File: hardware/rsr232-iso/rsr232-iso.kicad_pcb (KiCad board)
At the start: 2 copper layers, 51 x 23 mm, 17 parts, among them J1 Serial, J2 PWR, J3 data, U1 MAX3232, U2 TLP2358, U3 TLP2358

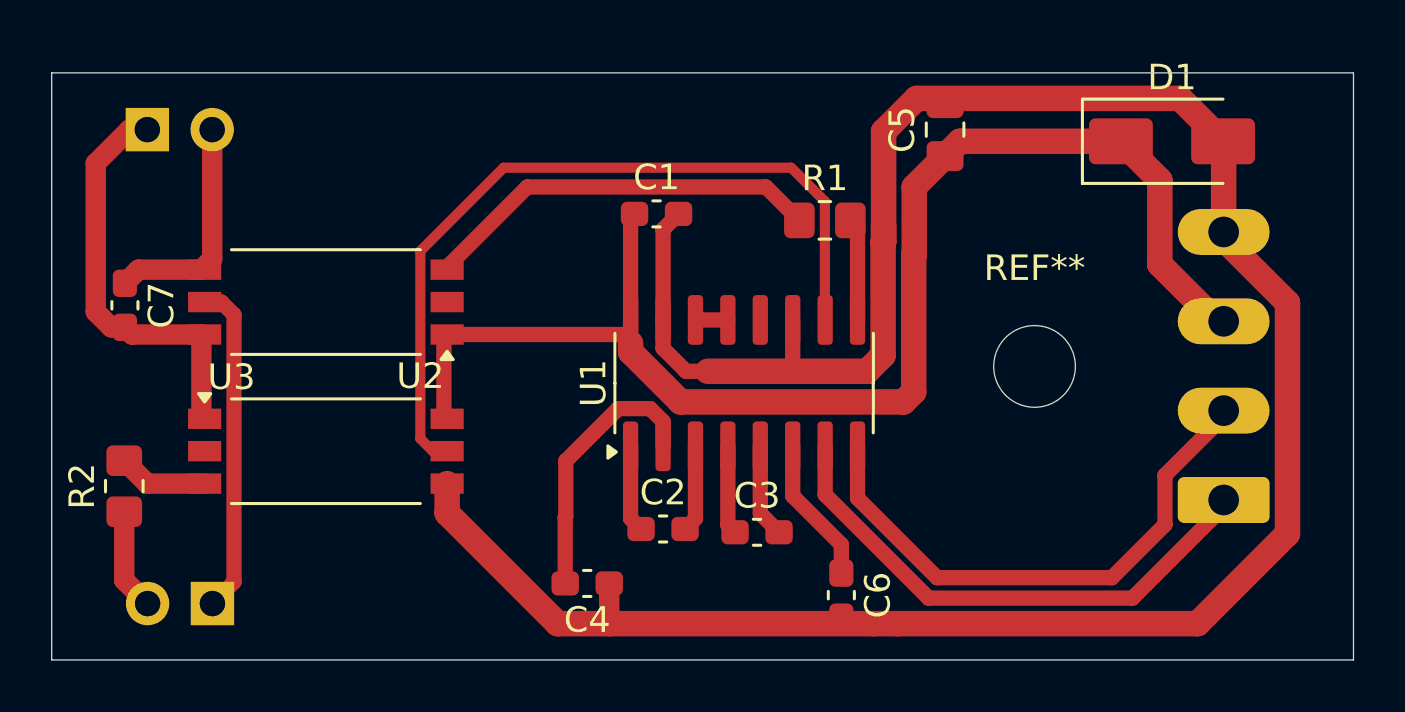
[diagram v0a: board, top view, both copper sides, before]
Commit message: Better clearance for mounting hole precise position for connectors
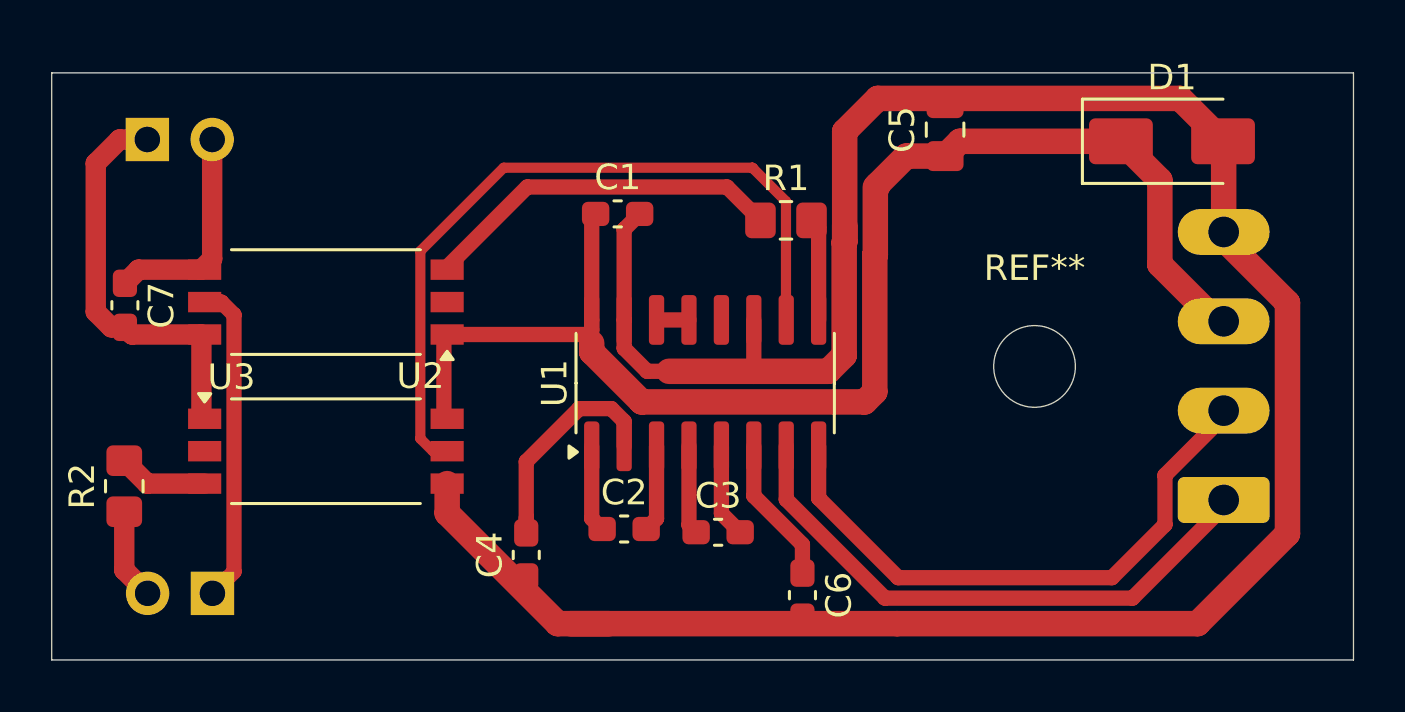
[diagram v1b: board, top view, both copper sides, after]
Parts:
- moved C4 2.64 mm to (143.1, 125.7), turned to 90 degrees
- moved C1 1.52 mm to (146.7, 112.4)
- moved C2 1.52 mm to (146.9, 124.7)
- moved C6 1.52 mm to (153.9, 127.3)
- moved R1 1.52 mm to (153.3, 112.6)
- moved U1 1.52 mm to (150.1, 119.0)
- moved C3 1.52 mm to (150.6, 124.8)
- moved J3 0.40 mm to (130.8, 127.2)
- moved J2 0.39 mm to (128.3, 109.5)
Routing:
- net /RS232tx: track 20.7 -> 22.3 mm
- net Net-(U2-K): track 15.8 -> 14.3 mm
- net /RS232rx: track 21.8 -> 23.3 mm
- net GND: track 96.1 -> 97.6 mm
- net Net-(U1-T2IN): track 31.0 -> 29.6 mm
- net Net-(U1-VS+): track 10.7 -> 9.28 mm

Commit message: Use a 2DIB1411F isolator instead of 2 optocouplers
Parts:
- removed R1: 330, Resistor_SMD:R_0805_2012Metric_Pad1.20x1.40mm_HandSolder
- removed R2: 220, Resistor_SMD:R_0805_2012Metric_Pad1.20x1.40mm_HandSolder
- removed REF**: MountingHole_3.2mm_M3_ISO7380, MountingHole:MountingHole_3.2mm_M3_ISO7380
- removed U3: TLP2358, Package_SO:SO-6L_10x3.84mm_P1.27mm
- added C8: 100nF, Capacitor_SMD:C_0603_1608Metric_Pad1.08x0.95mm_HandSolder, F.Cu at (141.4, 121.5)
- added H1: MountingHole, MountingHole:MountingHole_3.2mm_M3_DIN965, F.Cu at (162.9, 118.3)
- U2: value TLP2358 -> ADuM1201AR; footprint Package_SO:SO-6L_10x3.84mm_P1.27mm -> Package_SO:SOIC-8_3.9x4.9mm_P1.27mm
- moved U2 4.42 mm to (135.3, 120.2), turned to 0 degrees
- moved C7 2.09 mm to (128.9, 117.3), turned to 0 degrees
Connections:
- J3 pad 1: /RX -> /TX
- J3 pad 2: /TX -> /RX
- U2 pad 1: +5V -> +3.3V
- U2 pad 2: unconnected-(U2-NC-Pad2) -> /RX
- U2 pad 3: Net-(U2-K) -> /TX
- U2 pad 5: /RX -> GND
- U2 pad 6: +3.3V -> Net-(U1-T2IN)
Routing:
- net GNDD: track 8.49 -> 38.3 mm
- net Net-(U1-R2OUT): track 4.02 -> 28.0 mm
- net Net-(U2-K): track 14.3 -> 0.00 mm
- net +5V: track 53.6 -> 59.7 mm, vias 0 -> 2
- net /TX: track 3.58 -> 7.80 mm
- net +3.3V: track 16.1 -> 12.0 mm
- net Net-(U3-K): track 3.52 -> 0.00 mm
- net Net-(U1-T2IN): track 29.6 -> 26.8 mm
- net GND: track 97.6 -> 98.6 mm
- net /RX: track 12.7 -> 11.9 mm

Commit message: Cleanup PCB
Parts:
- U2: value ADuM1201AR -> 2DIB1411F
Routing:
- net +5V: track 59.7 -> 58.3 mm
- net Net-(U1-R2OUT): track 28.0 -> 27.4 mm
- net Net-(U1-VS+): track 9.28 -> 8.67 mm
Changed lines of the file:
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@@
 		(tags "capacitor handsolder")
 		(property "Reference" "C7"
-			(at 0 -1.43 360)
+			(at 0 -1.43 0)
 			(layer "F.SilkS")
 			(effects
@@
 		)
 		(property "Value" "100nF"
-			(at 0 1.43 360)
+			(at 0 1.43 0)
 			(layer "F.Fab")
 			(effects
@@
 		)
 		(fp_text user "${REFERENCE}"
-			(at 0 0 360)
+			(at 0 0 0)
 			(layer "F.Fab")
 			(effects
@@
 			)
 		)
-		(property "Value" "ADuM1201AR"
+		(property "Value" "2DIB1411F"
 			(at 0 3.4 0)
 			(layer "F.Fab")
@@
 			)
 		)
-		(property "Datasheet" "https://www.analog.com/media/en/technical-documentation/data-sheets/ADuM1200_1201.pdf"
+		(property "Datasheet" ""
 			(at 0 0 0)
 			(unlocked yes)
@@
 				(font
 					(size 1.27 1.27)
+				)
+			)
+		)
+		(property "P/N" "2DIB1411F"
+			(at 0 0 0)
+			(unlocked yes)
+			(layer "F.Fab")
+			(hide yes)
+			(effects
+				(font
+					(size 1 1)
+					(thickness 0.15)
 				)
 			)
@@
 	)
 	(segment
-		(start 145.669 117.7798)
-		(end 145.669 117.435238)
-		(width 1)
+		(start 145.6436 117.7544)
+		(end 145.669 117.7798)
+		(width 0.6)
 		(layer "F.Cu")
 		(net 1)
@@
 	)
 	(segment
-		(start 143.5608 115.7732)
-		(end 145.3642 115.7732)
-		(width 0.6)
-		(layer "F.Cu")
-		(net 1)
-	)
-	(segment
 		(start 167.9265 111.0493)
 		(end 166.402 109.5248)
@@
 	)
 	(segment
+		(start 143.5608 117.7544)
+		(end 145.6436 117.7544)
+		(width 0.6)
+		(layer "F.Cu")
+		(net 1)
+	)
+	(segment
 		(start 156.759 113.991686)
 		(end 156.759 119.339)
@@
 	)
 	(segment
-		(start 145.8225 112.3696)
-		(end 145.669 112.5231)
-		(width 0.6)
-		(layer "F.Cu")
-		(net 1)
-	)
-	(segment
-		(start 145.669 116.9162)
-		(end 145.4912 117.094)
-		(width 0.6)
-		(layer "F.Cu")
-		(net 1)
-	)
-	(segment
 		(start 170.4265 116.8505)
 		(end 167.9265 114.3505)
@@
 	)
 	(segment
-		(start 145.3642 115.7732)
-		(end 145.669 115.4684)
+		(start 143.5608 117.7544)
+		(end 143.5608 115.7732)
 		(width 0.6)
 		(layer "F.Cu")
@@
 	(segment
 		(start 143.5608 118.4667)
-		(end 143.5608 115.7732)
-		(width 0.6)
-		(layer "F.Cu")
-		(net 1)
-	)
-	(segment
-		(start 145.669 116.524)
-		(end 145.669 116.9162)
-		(width 0.6)
-		(layer "F.Cu")
-		(net 1)
-	)
-	(segment
-		(start 159.5335 110.0836)
-		(end 159.512 110.1051)
-		(width 1)
+		(end 143.5608 117.7544)
+		(width 0.6)
 		(layer "F.Cu")
 		(net 1)
@@
 	)
 	(segment
-		(start 169.40503 128.4224)
-		(end 157.6324 128.4224)
+		(start 144.8308 128.4224)
+		(end 169.40503 128.4224)
 		(width 1)
 		(layer "F.Cu")
@@
 	)
 	(segment
-		(start 157.6324 128.4224)
-		(end 144.8308 128.4224)
-		(width 1)
-		(layer "F.Cu")
-		(net 2)
-	)
-	(segment
 		(start 146.939 117.635586)
 		(end 147.839014 118.5356)
@@
 	)
 	(segment
-		(start 170.4265 109.5493)
-		(end 170.402 109.5248)
-		(width 1)
-		(layer "F.Cu")
-		(net 2)
-	)
-	(segment
 		(start 154.93447 118.5356)
 		(end 155.559 117.91107)
@@
 	)
 	(segment
-		(start 143.1036 124.8675)
-		(end 143.1058 124.8653)
-		(width 0.6)
-		(layer "F.Cu")
-		(net 7)
-	)
-	(segment
 		(start 145.177 119.999)
 		(end 143.1036 122.0724)
-		(width 0.6)
-		(layer "F.Cu")
-		(net 7)
-	)
-	(segment
-		(start 143.1058 124.8653)
-		(end 143.1058 124.2557)
 		(width 0.6)
 		(layer "F.Cu")
@@
 	)
 	(segment
-		(start 170.4265 120.309712)
-		(end 170.4265 120.0773)
-		(width 0.6)
-		(layer "F.Cu")
-		(net 12)
-	)
-	(segment
-		(start 170.4265 120.5051)
-		(end 170.4265 120.3505)
-		(width 0.6)
-		(layer "F.Cu")
-		(net 12)
-	)
-	(segment
 		(start 131.7498 120.8786)
 		(end 130.81 121.8184)
@@
 		(width 0.6)
 		(layer "F.Cu")
-		(net 18)
-	)
-	(segment
-		(start 138.4046 119.6086)
-		(end 137.7554 119.6086)
-		(width 0.6)
-		(layer "F.Cu")

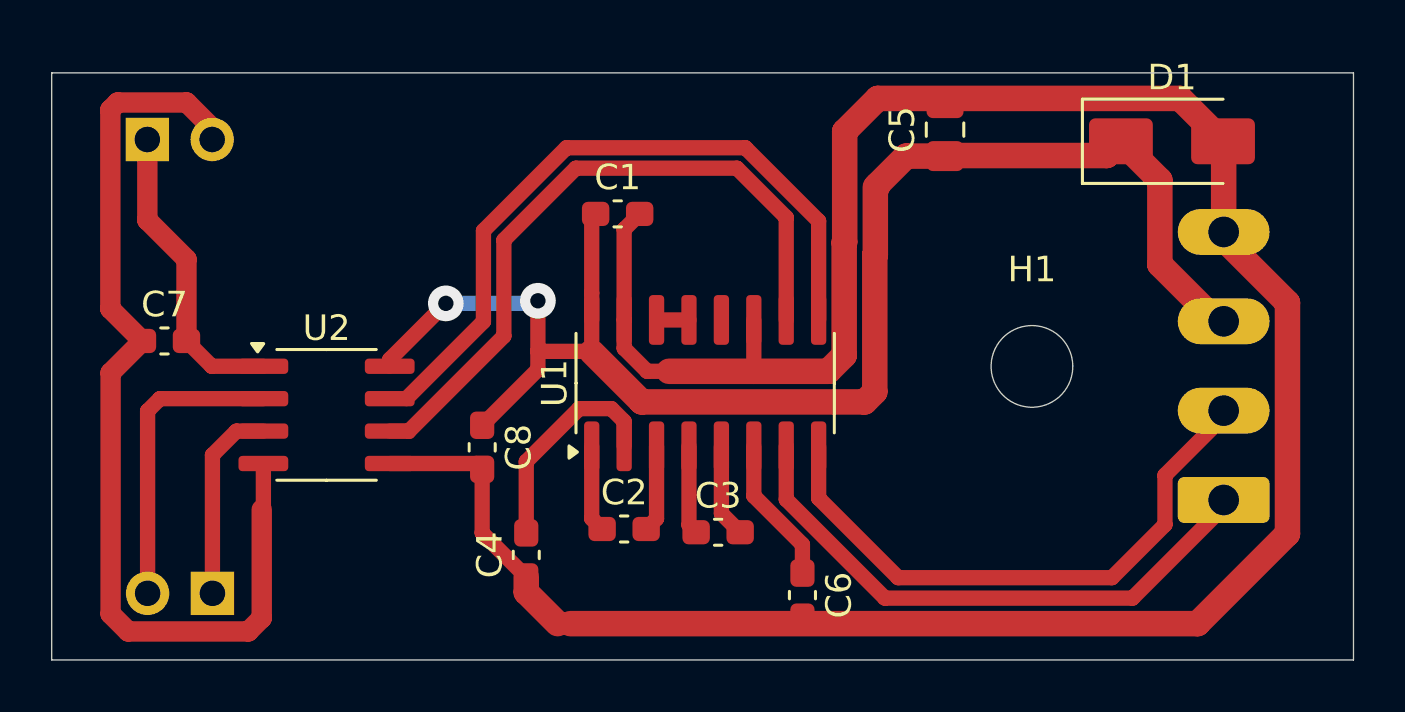
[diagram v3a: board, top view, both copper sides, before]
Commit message: energie, rsr232-iso: ajout des fichiers de fabrication
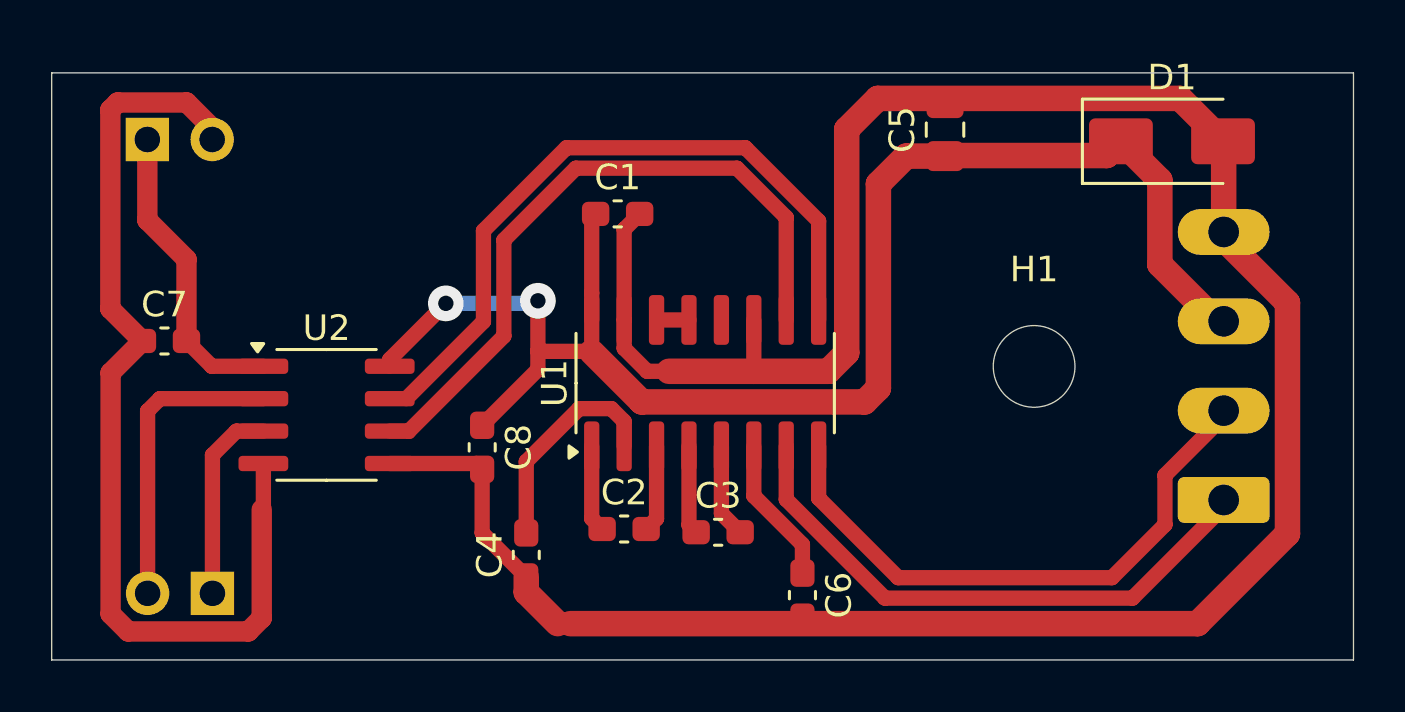
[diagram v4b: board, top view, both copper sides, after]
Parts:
- moved H1 0.08 mm to (163.0, 118.3)
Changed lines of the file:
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@@
 		(allow_soldermask_bridges_in_footprints no)
 		(pcbplotparams
-			(layerselection 0x00010fc_ffffffff)
+			(layerselection 0x0001080_7fffffff)
 			(plot_on_all_layers_selection 0x0000000_00000000)
 			(disableapertmacros no)
@@
 			(usegerberattributes yes)
 			(usegerberadvancedattributes yes)
-			(creategerberjobfile yes)
+			(creategerberjobfile no)
 			(dashed_line_dash_ratio 12.000000)
 			(dashed_line_gap_ratio 3.000000)
@@
 			(outputformat 1)
 			(mirror no)
-			(drillshape 1)
+			(drillshape 0)
 			(scaleselection 1)
-			(outputdirectory "")
+			(outputdirectory "fab")
 		)
 	)
@@
 	(footprint "MountingHole:MountingHole_3.2mm_M3_DIN965"
 		(layer "F.Cu")
-		(at 162.9156 118.3448)
+		(at 163 118.3448)
 		(descr "Mounting Hole 3.2mm, no annular, M3, DIN965")
 		(tags "mounting hole 3.2mm no annular m3 din965")
@@
 	)
 	(segment
-		(start 156.7796 113.971086)
-		(end 156.759 113.991686)
-		(width 1)
-		(layer "F.Cu")
-		(net 1)
-	)
-	(segment
 		(start 145.6436 117.7544)
 		(end 145.669 117.7798)
@@
 	)
 	(segment
-		(start 156.8597 111.2334)
-		(end 156.8597 111.3135)
-		(width 1)
-		(layer "F.Cu")
-		(net 1)
-	)
-	(segment
-		(start 156.759 119.339)
-		(end 156.3624 119.7356)
-		(width 1)
-		(layer "F.Cu")
-		(net 1)
-	)
-	(segment
-		(start 156.7796 111.3135)
-		(end 156.7796 113.971086)
+		(start 156.3624 119.7356)
+		(end 156.9 119.198)
 		(width 1)
 		(layer "F.Cu")
@@
 	)
 	(segment
-		(start 159.512 110.1051)
-		(end 157.988 110.1051)
-		(width 1)
-		(layer "F.Cu")
-		(net 1)
-	)
-	(segment
 		(start 145.669 115.4684)
 		(end 145.669 116.524)
@@
 	)
 	(segment
-		(start 147.6248 119.7356)
-		(end 145.669 117.7798)
-		(width 1)
-		(layer "F.Cu")
-		(net 1)
-	)
-	(segment
 		(start 145.669 112.5231)
 		(end 145.669 115.4684)
@@
 	)
 	(segment
-		(start 156.759 113.991686)
-		(end 156.759 119.339)
-		(width 1)
-		(layer "F.Cu")
-		(net 1)
-	)
-	(segment
 		(start 170.4265 116.8505)
 		(end 167.9265 114.3505)
@@
 	)
 	(segment
-		(start 157.988 110.1051)
-		(end 156.8597 111.2334)
+		(start 147.6248 119.7356)
+		(end 156.3624 119.7356)
 		(width 1)
 		(layer "F.Cu")
@@
 	)
 	(segment
-		(start 156.3624 119.7356)
+		(start 156.9 111.1931)
+		(end 157.988 110.1051)
+		(width 1)
+		(layer "F.Cu")
+		(net 1)
+	)
+	(segment
+		(start 145.669 117.7798)
 		(end 147.6248 119.7356)
 		(width 1)
@@
 		(net 1)
 	)
+	(segment
+		(start 156.9 119.198)
+		(end 156.9 111.1931)
+		(width 1)
+		(layer "F.Cu")
+		(net 1)
+	)
+	(segment
+		(start 157.988 110.1051)
+		(end 159.512 110.1051)
+		(width 1)
+		(layer "F.Cu")
+		(net 1)
+	)
 	(via
 		(at 143.5608 115.7732)
@@
 	)
 	(segment
+		(start 154.93447 118.5356)
+		(end 155.659 117.81107)
+		(width 1)
+		(layer "F.Cu")
+		(net 2)
+	)
+	(segment
 		(start 144.8308 128.4224)
 		(end 169.40503 128.4224)
@@
 	)
 	(segment
+		(start 151.9936 118.5356)
+		(end 154.93447 118.5356)
+		(width 1)
+		(layer "F.Cu")
+		(net 2)
+	)
+	(segment
 		(start 170.4265 113.3505)
 		(end 172.9265 115.8505)
@@
 	)
 	(segment
-		(start 168.722 107.8448)
+		(start 155.659 109.0598)
 		(end 156.874 107.8448)
 		(width 1)
@@
 	)
 	(segment
-		(start 170.402 109.5248)
-		(end 168.722 107.8448)
-		(width 1)
-		(layer "F.Cu")
-		(net 2)
-	)
-	(segment
-		(start 156.874 107.8448)
-		(end 155.5796 109.1392)
-		(width 1)
-		(layer "F.Cu")
-		(net 2)
-	)
-	(segment
-		(start 155.5796 113.47403)
-		(end 155.559 113.49463)
+		(start 168.722 107.8448)
+		(end 170.402 109.5248)
 		(width 1)
 		(layer "F.Cu")
@@
 	)
 	(segment
+		(start 156.874 107.8448)
+		(end 168.722 107.8448)
+		(width 1)
+		(layer "F.Cu")
+		(net 2)
+	)
+	(segment
 		(start 146.939 116.524)
 		(end 146.939 112.9781)
@@
 	)
 	(segment
-		(start 155.559 117.91107)
-		(end 155.559 113.49463)
+		(start 155.659 117.81107)
+		(end 155.659 109.0598)
 		(width 1)
 		(layer "F.Cu")
@@
 	)
 	(segment
-		(start 154.93447 118.5356)
-		(end 155.559 117.91107)
-		(width 1)
-		(layer "F.Cu")
-		(net 2)
-	)
-	(segment
 		(start 147.839014 118.5356)
 		(end 148.6916 118.5356)
@@
 	)
 	(segment
-		(start 151.9936 118.5356)
-		(end 154.93447 118.5356)
-		(width 1)
-		(layer "F.Cu")
-		(net 2)
-	)
-	(segment
 		(start 146.939 116.524)
 		(end 146.939 117.635586)
@@
 		(layer "F.Cu")
 		(net 2)
-	)
-	(segment
-		(start 155.5796 109.1392)
-		(end 155.5796 113.47403)
-		(width 1)
-		(layer "F.Cu")
-		(net 2)
